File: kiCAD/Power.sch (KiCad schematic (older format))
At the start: 0 parts

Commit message: Completed Schematic, assigned footprints.
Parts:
- added C106, C107, C112, C113, C124, C125, C126, C135: 100n, Capacitor_SMD:C_0603_1608Metric_Pad1.05x0.95mm_HandSolder, symbol Device:C_Small
- added C108, C109: 1n, Capacitor_SMD:C_0603_1608Metric_Pad1.05x0.95mm_HandSolder, symbol Device:C_Small
- added C110, C111, C127, C134: 10u, Capacitor_SMD:C_1206_3216Metric_Pad1.42x1.75mm_HandSolder, symbol Device:C_Small
- added C114, C115, C116, C117: 4.7u, Capacitor_SMD:C_0603_1608Metric_Pad1.05x0.95mm_HandSolder, symbol Device:C_Small
- added C118: 2n, Capacitor_SMD:C_0603_1608Metric_Pad1.05x0.95mm_HandSolder, symbol Device:C_Small
- added C119: 2.2n, Capacitor_SMD:C_0603_1608Metric_Pad1.05x0.95mm_HandSolder, symbol Device:C_Small
- added C120, C121: 22p, Capacitor_SMD:C_0603_1608Metric_Pad1.05x0.95mm_HandSolder, symbol Device:C_Small
- added C122, C123: 10n, Capacitor_SMD:C_0603_1608Metric_Pad1.05x0.95mm_HandSolder, symbol Device:C_Small
- added C128, C129: 47p, Capacitor_SMD:C_0603_1608Metric_Pad1.05x0.95mm_HandSolder, symbol Device:C_Small
- added C130, C131, C132, C133: 47u, Capacitor_SMD:C_1210_3225Metric_Pad1.42x2.65mm_HandSolder, symbol Device:C_Small
- added D1, D2: SMAJ24, Diode_SMD:D_SMA_Handsoldering, symbol Device:D_TVS
- added D10, D11, D3, D4: LED_Small, Diode_SMD:D_0603_1608Metric_Pad1.05x0.95mm_HandSolder, symbol Device:LED_Small
- added D12: G, Diode_SMD:D_0603_1608Metric_Pad1.05x0.95mm_HandSolder, symbol Device:LED_Small
- added D5, D6, D7: SK56A-TP, Diode_SMD:D_SMA_Handsoldering, symbol Device:D_Schottky
- added D8, D9: B540, Diode_SMD:D_SMC_Handsoldering, symbol Device:D_Schottky
- added F2: 7A - TBD, Fuse:Fuseholder_Blade_Mini_Keystone_3568, symbol Device:Fuse
- added F3: 15A, Fuse:Fuseholder_Blade_Mini_Keystone_3568, symbol Device:Fuse
- added F4, F5: 5A, Fuse:Fuse_2920_7451Metric_Pad2.10x5.45mm_HandSolder, symbol Device:Fuse
- added J10: MAIN_POWER, TerminalBlock_Dinkle:TerminalBlock_Dinkle_DT-55-B01X-02_P10.00mm, symbol Connector_Generic:Conn_01x02
- added J11: BED_POWER, TerminalBlock_Dinkle:TerminalBlock_Dinkle_DT-55-B01X-02_P10.00mm, symbol Connector_Generic:Conn_01x02
- added JP2: SELECT, Connector_PinHeader_2.54mm:PinHeader_1x03_P2.54mm_Vertical, symbol Jumper:Jumper_3_Open
- added L1, L2: 4.7u, Inductor_SMD:L_Vishay_IHLP-2525, symbol Device:L_Small
- added R33, R34, R35, R37, R41, R42, R43: 10k, Resistor_SMD:R_0603_1608Metric_Pad1.05x0.95mm_HandSolder, symbol Device:R_Small_US
- added R36: 37.4k, Resistor_SMD:R_0603_1608Metric_Pad1.05x0.95mm_HandSolder, symbol Device:R_Small_US
- added R38: 1.42k, Resistor_SMD:R_0603_1608Metric_Pad1.05x0.95mm_HandSolder, symbol Device:R_Small_US
- added R39: 10.2k, Resistor_SMD:R_0603_1608Metric_Pad1.05x0.95mm_HandSolder, symbol Device:R_Small_US
- added R40: 1.96k, Resistor_SMD:R_0603_1608Metric_Pad1.05x0.95mm_HandSolder, symbol Device:R_Small_US
- added U10, U11: TPS54531, Package_SO:TI_SO-PowerPAD-8_ThermalVias, symbol Power_and_Buck_Converters:TPS54531
- added U12: AP7361C-33E-13, Package_TO_SOT_SMD:SOT-223, symbol Power_and_Buck_Converters:AP7361C-33E-13
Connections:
- new net: C124.2, U10.1 (BOOT)
- new net: C112.1, C114.1, C116.1, D6.1 (K), U10.2 (V_IN)
- new net: C122.1, U10.4 (SS)
- new net: C128.2, R37.2, R38.1, U10.5 (V_SENSE)
- new net: C118.1, C120.1, U10.6 (COMP)
- new net: C124.1, D8.1 (K), L1.1, U10.8 (PH)
- new net: C126.1, C127.1, JP2.2 (C), U12.1 (IN)
- new net: F2.2, J10.2 (Pin_2)
- new net: F3.2, J11.2 (Pin_2)
- new net: C118.2, R35.1
- new net: C128.1, C130.1, C132.1, F4.2, L1.2, R37.1
- new net: C125.2, U11.1 (BOOT)
- new net: C113.1, C115.1, C117.1, D7.1 (K), U11.2 (V_IN)
- new net: C123.1, U11.4 (SS)
- new net: C129.2, R39.2, R40.1, U11.5 (V_SENSE)
- new net: C119.1, C121.1, U11.6 (COMP)
- new net: C125.1, D9.1 (K), L2.1, U11.8 (PH)
- new net: C119.2, R36.1
- new net: C129.1, C131.1, C133.1, F5.2, L2.2, R39.1
- new net: D10.2 (A), R41.2
- new net: D11.2 (A), R42.2
- new net: D12.2 (A), R43.2
- new net: D3.2 (A), R33.2
- new net: D4.2 (A), R34.2
- new net +12V: F4.1, R41.1
- new net +24V: C106.1, C108.1, C110.1, D1.1 (A1), D5.2 (A), D6.2 (A), D7.2 (A), F2.1, R33.1
- new net +3V3: C134.1, C135.1, R43.1, U12.3 (OUT)
- new net +5V: F5.1, JP2.3 (B), R42.1
- new net GND: C106.2, C107.2, C108.2, C109.2, C110.2, C111.2, C112.2, C113.2, C114.2, C115.2, C116.2, C117.2, C120.2, C121.2, C122.2, C123.2, C126.2, C127.2, C130.2, C131.2, C132.2, C133.2, C134.2, C135.2, D1.2 (A2), D10.1 (K), D11.1 (K), D12.1 (K), D2.2 (A2), D3.1 (K), D4.1 (K), D8.2 (A), D9.2 (A), J10.1 (Pin_1), J11.1 (Pin_1), R35.2, R36.2, R38.2, R40.2, U10.7 (GND), U10.9 (PAD), U11.7 (GND), U11.9 (PAD), U12.2 (GND), U12.4 (PAD)
- new net VBED: C107.1, C109.1, C111.1, D2.1 (A1), F3.1, R34.1
- new net VBUS: JP2.1 (A)
- new net VM: D5.1 (K)
- no-connect marks 0 -> 2
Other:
- note added: "47u - 1210X476K160CT"
- note added: "HIGH POWER BUCK CONVERTERS\n"
- note added: "IHLP2525EZER4R7M01"
- note added: "IMPORTANT DECISION - LED COLOURS"
- note added: "LOW POWER BUCK CONVERTERS\n"
- note added: "POWER INPUTS\n"

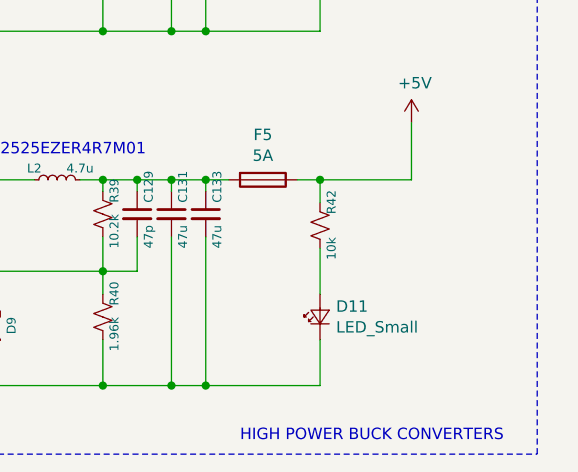
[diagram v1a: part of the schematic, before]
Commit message: added power plane
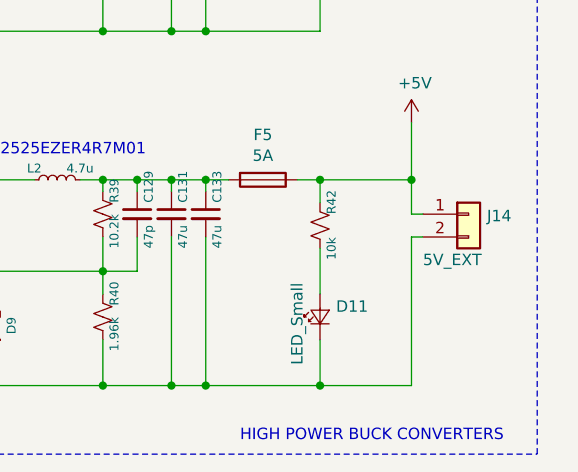
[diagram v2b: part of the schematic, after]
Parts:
- added J14: 5V_EXT, Connector_Molex:Molex_KK-254_AE-6410-02A_1x02_P2.54mm_Vertical, symbol Connector_Generic:Conn_01x02
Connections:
- net +5V: now also J14.1 (Pin_1)
- net GND: now also J14.2 (Pin_2)
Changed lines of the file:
@@
 P 8900 5150
 F 0 "D11" V 8946 5080 50  0000 R CNN
-F 1 "LED_Small" V 8855 5080 50  0000 R CNN
+F 1 "LED_Small" H 9050 5250 50  0000 R CNN
 F 2 "Diode_SMD:D_0603_1608Metric_Pad1.05x0.95mm_HandSolder" V 8900 5150 50  0001 C CNN
 F 3 "~" V 8900 5150 50  0001 C CNN
@@
 Wire Notes Line
 	6900 2400 9850 2400
+$Comp
+L Connector_Generic:Conn_01x02 J14
+U 1 1 5FC193AD
+P 9550 4700
+F 0 "J14" H 9630 4692 50  0000 L CNN
+F 1 "5V_EXT" H 9350 4500 50  0000 L CNN
+F 2 "Connector_Molex:Molex_KK-254_AE-6410-02A_1x02_P2.54mm_Vertical" H 9550 4700 50  0001 C CNN
+F 3 "~" H 9550 4700 50  0001 C CNN
+	1    9550 4700
+	1    0    0    -1
+$EndComp
+Wire Wire Line
+	9350 4700 9300 4700
+Wire Wire Line
+	9300 4700 9300 4550
+Connection ~ 9300 4550
+Wire Wire Line
+	8900 5450 9300 5450
+Wire Wire Line
+	9300 5450 9300 4800
+Wire Wire Line
+	9300 4800 9350 4800
+Connection ~ 8900 5450
 $EndSCHEMATC
